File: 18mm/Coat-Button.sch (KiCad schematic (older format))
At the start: 41 parts, among them IC1 MADW__ATTINY13-MM, P1 CONN_1, P2 CONN_1, P3 CONN_1, P4 CONN_1, Q1 DMG1012T, Q2 DMG1012T

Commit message: Tweaked changes in previous commit.
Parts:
- added JP2, JP3: JUMPER, symbol JUMPER
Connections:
- wire segments 83 -> 93
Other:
- note added: "cut if transistors are used!"
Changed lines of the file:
@@
 Sheet 1 1
 Title "Coat-Button"
-Date "03 Oct 2013"
-Rev "0.22"
+Date "14 Oct 2013"
+Rev "0.23"
 Comp "2013 - blog.spitzenpfeil.org"
 Comment1 ""
@@
 Text GLabel 3350 2900 0    39   Input ~ 0
 SCK
-Wire Wire Line
-	4950 1700 5200 1700
-Wire Wire Line
-	4950 2000 5200 2000
-Connection ~ 5000 2000
-Connection ~ 5000 1700
-Wire Wire Line
-	5450 2700 5700 2700
-Wire Wire Line
-	5700 2600 5700 2750
-Wire Wire Line
-	5450 3200 5700 3200
-Wire Wire Line
-	5700 3150 5700 3300
-Connection ~ 5700 2700
-Connection ~ 5700 3200
-Wire Wire Line
-	3400 1650 3250 1650
-Wire Wire Line
-	3250 1750 3400 1750
-Wire Wire Line
-	3250 1850 3400 1850
-Wire Wire Line
-	4000 1650 4150 1650
-Wire Wire Line
-	4000 1750 4150 1750
-Wire Wire Line
-	4000 1850 4150 1850
-Wire Wire Line
-	4150 1650 4150 1550
-Wire Wire Line
-	4150 1850 4150 1950
-Wire Wire Line
-	3450 2700 3350 2700
-Wire Wire Line
-	3300 3200 3450 3200
-Wire Wire Line
-	3350 2800 3450 2800
-Wire Wire Line
-	3350 2900 3450 2900
-Wire Wire Line
-	5000 1900 5000 2100
-Wire Wire Line
-	5000 1600 5000 1800
-Wire Wire Line
-	5000 1800 4950 1800
-Wire Wire Line
-	3150 3000 3450 3000
-Wire Wire Line
-	3450 3100 3150 3100
 Text Label 3150 3000 2    60   ~ 0
 gate_a
-Wire Wire Line
-	4950 1900 5000 1900
 $Comp
 L CONN_1 P1
@@
 	0    1    1    0
 $EndComp
-Wire Wire Line
-	2300 4350 2300 4250
-Wire Wire Line
-	2300 4250 7400 4250
-Wire Wire Line
-	7400 4250 7400 4350
-Wire Wire Line
-	7200 4350 7200 4250
-Connection ~ 7200 4250
-Wire Wire Line
-	6700 4350 6700 4250
-Connection ~ 6700 4250
-Wire Wire Line
-	6500 4350 6500 4250
-Connection ~ 6500 4250
-Wire Wire Line
-	6000 4350 6000 4250
-Connection ~ 6000 4250
-Wire Wire Line
-	5800 4350 5800 4250
-Connection ~ 5800 4250
-Wire Wire Line
-	5300 4350 5300 4250
-Connection ~ 5300 4250
-Wire Wire Line
-	5100 4350 5100 4250
-Connection ~ 5100 4250
-Wire Wire Line
-	4600 4350 4600 4250
-Connection ~ 4600 4250
-Wire Wire Line
-	4400 4350 4400 4250
-Connection ~ 4400 4250
-Wire Wire Line
-	3900 4350 3900 4250
-Connection ~ 3900 4250
-Wire Wire Line
-	3700 4350 3700 4250
-Connection ~ 3700 4250
-Wire Wire Line
-	3200 4350 3200 4250
-Connection ~ 3200 4250
-Wire Wire Line
-	3000 4350 3000 4250
-Connection ~ 3000 4250
-Wire Wire Line
-	2500 4350 2500 4250
-Connection ~ 2500 4250
 $Comp
 L R R1.1
@@
 	-1   0    0    1
 $EndComp
-Wire Wire Line
-	2300 5350 2300 5500
-Wire Wire Line
-	3000 5500 3000 5350
-Wire Wire Line
-	3700 5500 3700 5350
-Connection ~ 3000 5500
-Wire Wire Line
-	4400 5500 4400 5350
-Connection ~ 3700 5500
-Wire Wire Line
-	7200 5500 7200 5350
-Connection ~ 4400 5500
-Wire Wire Line
-	6500 5350 6500 5500
-Connection ~ 6500 5500
-Wire Wire Line
-	5800 5350 5800 5500
-Connection ~ 5800 5500
-Wire Wire Line
-	5100 5350 5100 5500
-Connection ~ 5100 5500
-Wire Wire Line
-	2500 5350 2500 5600
-Wire Wire Line
-	2500 5600 8300 5600
-Wire Wire Line
-	3200 5600 3200 5350
-Wire Wire Line
-	3900 5600 3900 5350
-Connection ~ 3200 5600
-Wire Wire Line
-	4600 5600 4600 5350
-Connection ~ 3900 5600
-Wire Wire Line
-	7400 5600 7400 5350
-Connection ~ 4600 5600
-Wire Wire Line
-	6700 5350 6700 5600
-Connection ~ 6700 5600
-Wire Wire Line
-	6000 5350 6000 5600
-Connection ~ 6000 5600
-Wire Wire Line
-	5300 5350 5300 5600
-Connection ~ 5300 5600
-Connection ~ 7200 5500
-Connection ~ 7400 5600
 Text Label 3150 3100 2    60   ~ 0
 gate_b
@@
 	1    0    0    -1
 $EndComp
-Wire Wire Line
-	8300 6100 9000 6100
-Wire Wire Line
-	9000 6100 9000 5950
-Wire Wire Line
-	8650 6100 8650 6200
-Connection ~ 8650 6100
 $Comp
 L GND #PWR010
@@
 	1    0    0    -1
 $EndComp
-Wire Wire Line
-	2300 5500 9000 5500
-Wire Wire Line
-	9000 5500 9000 5550
-Wire Wire Line
-	8300 5600 8300 5650
-Wire Wire Line
-	8300 6050 8300 6100
 Text Label 7950 5950 1    60   ~ 0
 gate_a
 Text Label 8650 5850 1    60   ~ 0
 gate_b
-Wire Wire Line
-	8650 5850 8700 5850
-Wire Wire Line
-	7950 5950 8000 5950
-Text Notes 2500 5700 0    39   ~ 0
+Text Notes 2250 5750 0    39   ~ 0
 * Adjust R for about 10mA per LED\n\n(*) Rx.2 alternate footprint for single-color LED. Use instead of Rx and Rx.1
 $Comp
@@
 	1    0    0    -1
 $EndComp
-Wire Wire Line
-	2500 4850 2600 4850
-Wire Wire Line
-	2500 5350 2600 5350
-Wire Wire Line
-	3200 5350 3300 5350
-Wire Wire Line
-	3200 4850 3300 4850
-Wire Wire Line
-	3900 4850 4000 4850
-Wire Wire Line
-	3900 5350 4000 5350
 Text Notes 2650 5000 0    39   ~ 0
 (*)
 Wire Wire Line
+	4950 1700 5200 1700
+Wire Wire Line
+	4950 2000 5200 2000
+Connection ~ 5000 2000
+Connection ~ 5000 1700
+Wire Wire Line
+	5450 2700 5700 2700
+Wire Wire Line
+	5700 2600 5700 2750
+Wire Wire Line
+	5450 3200 5700 3200
+Wire Wire Line
+	5700 3150 5700 3300
+Connection ~ 5700 2700
+Connection ~ 5700 3200
+Wire Wire Line
+	3400 1650 3250 1650
+Wire Wire Line
+	3250 1750 3400 1750
+Wire Wire Line
+	3250 1850 3400 1850
+Wire Wire Line
+	4000 1650 4150 1650
+Wire Wire Line
+	4000 1750 4150 1750
+Wire Wire Line
+	4000 1850 4150 1850
+Wire Wire Line
+	4150 1650 4150 1550
+Wire Wire Line
+	4150 1850 4150 1950
+Wire Wire Line
+	3450 2700 3350 2700
+Wire Wire Line
+	3300 3200 3450 3200
+Wire Wire Line
+	3350 2800 3450 2800
+Wire Wire Line
+	3350 2900 3450 2900
+Wire Wire Line
+	5000 1900 5000 2100
+Wire Wire Line
+	5000 1600 5000 1800
+Wire Wire Line
+	5000 1800 4950 1800
+Wire Wire Line
+	3150 3000 3450 3000
+Wire Wire Line
+	3450 3100 3150 3100
+Wire Wire Line
+	4950 1900 5000 1900
+Wire Wire Line
+	2300 4350 2300 4250
+Wire Wire Line
+	2300 4250 7400 4250
+Wire Wire Line
+	7400 4250 7400 4350
+Wire Wire Line
+	7200 4350 7200 4250
+Connection ~ 7200 4250
+Wire Wire Line
+	6700 4350 6700 4250
+Connection ~ 6700 4250
+Wire Wire Line
+	6500 4350 6500 4250
+Connection ~ 6500 4250
+Wire Wire Line
+	6000 4350 6000 4250
+Connection ~ 6000 4250
+Wire Wire Line
+	5800 4350 5800 4250
+Connection ~ 5800 4250
+Wire Wire Line
+	5300 4350 5300 4250
+Connection ~ 5300 4250
+Wire Wire Line
+	5100 4350 5100 4250
+Connection ~ 5100 4250
+Wire Wire Line
+	4600 4350 4600 4250
+Connection ~ 4600 4250
+Wire Wire Line
+	4400 4350 4400 4250
+Connection ~ 4400 4250
+Wire Wire Line
+	3900 4350 3900 4250
+Connection ~ 3900 4250
+Wire Wire Line
+	3700 4350 3700 4250
+Connection ~ 3700 4250
+Wire Wire Line
+	3200 4350 3200 4250
+Connection ~ 3200 4250
+Wire Wire Line
+	3000 4350 3000 4250
+Connection ~ 3000 4250
+Wire Wire Line
+	2500 4350 2500 4250
+Connection ~ 2500 4250
+Wire Wire Line
+	2300 5350 2300 5500
+Wire Wire Line
+	3000 5500 3000 5350
+Wire Wire Line
+	3700 5500 3700 5350
+Connection ~ 3000 5500
+Wire Wire Line
+	4400 5500 4400 5350
+Connection ~ 3700 5500
+Wire Wire Line
+	7200 5500 7200 5350
+Connection ~ 4400 5500
+Wire Wire Line
+	6500 5350 6500 5500
+Connection ~ 6500 5500
+Wire Wire Line
+	5800 5350 5800 5500
+Connection ~ 5800 5500
+Wire Wire Line
+	5100 5350 5100 5800
+Connection ~ 5100 5500
+Wire Wire Line
+	2500 5350 2500 5600
+Wire Wire Line
+	2500 5600 8300 5600
+Wire Wire Line
+	3200 5600 3200 5350
+Wire Wire Line
+	3900 5600 3900 5350
+Connection ~ 3200 5600
+Wire Wire Line
+	4600 5600 4600 5350
+Connection ~ 3900 5600
+Wire Wire Line
+	7400 5600 7400 5350
+Connection ~ 4600 5600
+Wire Wire Line
+	6700 5350 6700 5600
+Connection ~ 6700 5600
+Connection ~ 6000 5600
+Wire Wire Line
+	5300 5350 5300 5600
+Connection ~ 5300 5600
+Connection ~ 7200 5500
+Connection ~ 7400 5600
+Wire Wire Line
+	8300 6100 9000 6100
+Wire Wire Line
+	9000 6100 9000 5950
+Wire Wire Line
+	8650 6100 8650 6200
+Connection ~ 8650 6100
+Wire Wire Line
+	2300 5500 9000 5500
+Wire Wire Line
+	9000 5500 9000 5550
+Wire Wire Line
+	8300 5600 8300 5650
+Wire Wire Line
+	8300 6050 8300 6100
+Wire Wire Line
+	8650 5850 8700 5850
+Wire Wire Line
+	7950 5950 8000 5950
+Wire Wire Line
+	2500 4850 2600 4850
+Wire Wire Line
+	2500 5350 2600 5350
+Wire Wire Line
+	3200 5350 3300 5350
+Wire Wire Line
+	3200 4850 3300 4850
+Wire Wire Line
+	3900 4850 4000 4850
+Wire Wire Line
+	3900 5350 4000 5350
+Wire Wire Line
 	4600 4850 4700 4850
 Wire Wire Line
@@
 Wire Wire Line
 	7400 5350 7500 5350
+$Comp
+L JUMPER JP3
+U 1 1 525C0CD5
+P 6000 6100
+F 0 "JP3" H 6000 6250 60  0000 C CNN
+F 1 "JUMPER" H 6000 6020 40  0000 C CNN
+F 2 "" H 6000 6100 60  0000 C CNN
+F 3 "" H 6000 6100 60  0000 C CNN
+	1    6000 6100
+	0    1    1    0
+$EndComp
+Wire Wire Line
+	6000 6400 6000 6500
+Wire Wire Line
+	5100 6400 5100 6500
+Text Label 6100 6500 0    60   ~ 0
+gate_a
+Text Label 5200 6500 0    60   ~ 0
+gate_b
+Wire Wire Line
+	6000 6500 6100 6500
+Wire Wire Line
+	5100 6500 5200 6500
+Wire Wire Line
+	5800 5800 5800 6400
+Wire Wire Line
+	5800 6400 6000 6400
+Wire Wire Line
+	6000 5350 6000 5800
+Wire Wire Line
+	6000 5800 5800 5800
+Wire Wire Line
+	5100 5800 4900 5800
+Wire Wire Line
+	4900 5800 4900 6400
+Wire Wire Line
+	4900 6400 5100 6400
+Text Notes 4050 6400 0    39   ~ 0
+cut if transistors are used!
+$Comp
+L JUMPER JP2
+U 1 1 525C1412
+P 5100 6100
+F 0 "JP2" H 5100 6250 60  0000 C CNN
+F 1 "JUMPER" H 5100 6020 40  0000 C CNN
+F 2 "" H 5100 6100 60  0000 C CNN
+F 3 "" H 5100 6100 60  0000 C CNN
+	1    5100 6100
+	0    1    1    0
+$EndComp
 $EndSCHEMATC

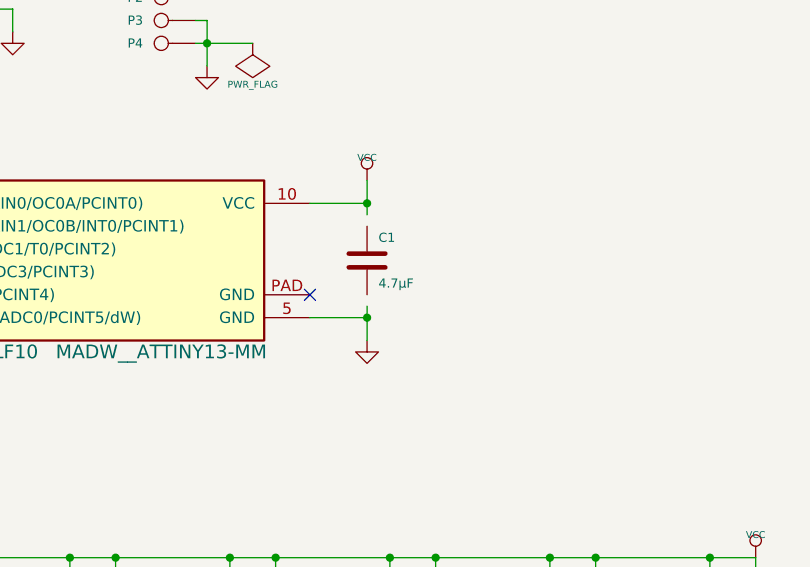
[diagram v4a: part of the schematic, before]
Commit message: Moved capacitor + tweaks.
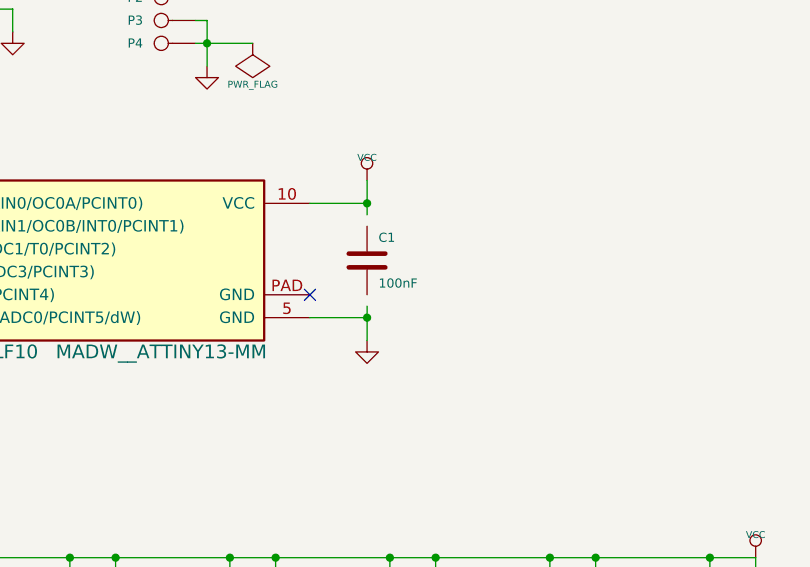
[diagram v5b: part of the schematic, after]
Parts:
- C1: value 4.7µF -> 100nF
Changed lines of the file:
@@
 P 5700 2950
 F 0 "C1" H 5750 3050 40  0000 L CNN
-F 1 "4.7µF" H 5750 2850 40  0000 L CNN
+F 1 "100nF" H 5750 2850 40  0000 L CNN
 F 2 "" H 5738 2800 30  0000 C CNN
 F 3 "" H 5700 2950 60  0000 C CNN

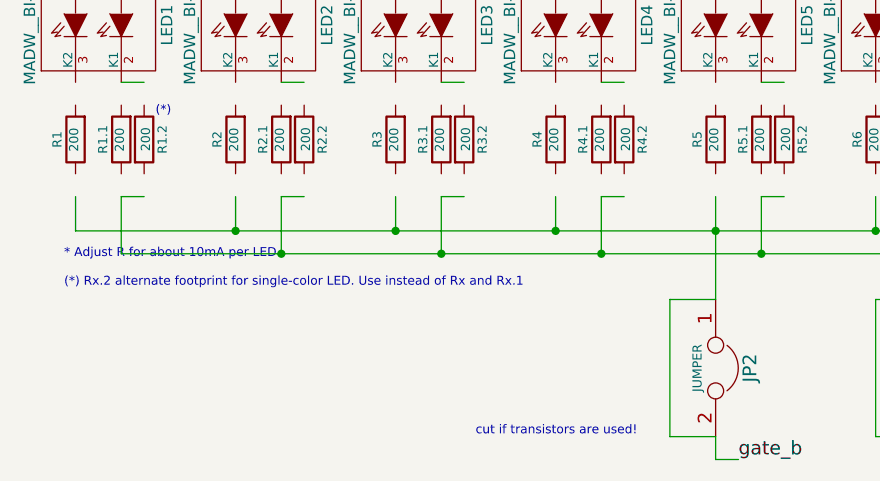
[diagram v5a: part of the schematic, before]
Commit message: Added a comment to the schematic (LED resistors).
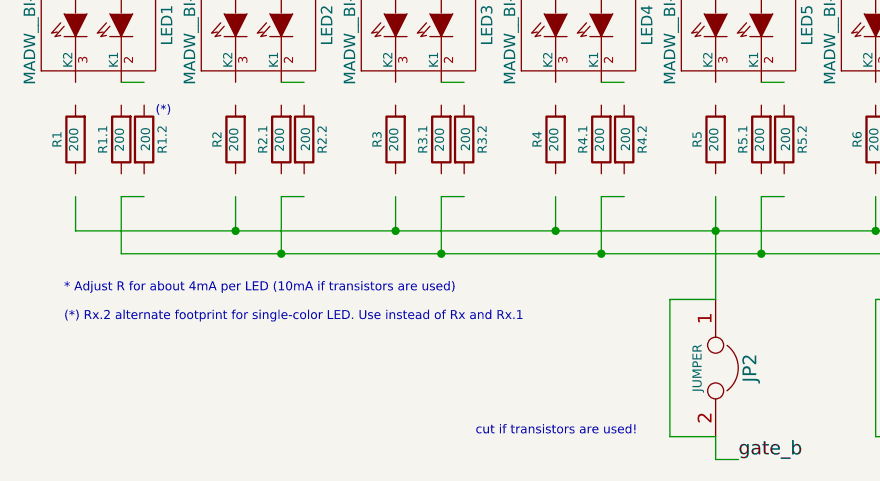
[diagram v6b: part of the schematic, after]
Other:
- note added: "* Adjust R for about 4mA per LED (10mA if transistors are used)\n\n(*) Rx.2 alternate footprint for single-color LED. Use instead of Rx and Rx.1"
- note removed: "* Adjust R for about 10mA per LED\n\n(*) Rx.2 alternate footprint for single-color LED. Use instead of Rx and Rx.1"
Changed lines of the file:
@@
 Text Label 8650 5850 1    60   ~ 0
 gate_b
-Text Notes 2250 5750 0    39   ~ 0
-* Adjust R for about 10mA per LED\n\n(*) Rx.2 alternate footprint for single-color LED. Use instead of Rx and Rx.1
+Text Notes 2250 5900 0    39   ~ 0
+* Adjust R for about 4mA per LED (10mA if transistors are used)\n\n(*) Rx.2 alternate footprint for single-color LED. Use instead of Rx and Rx.1
 $Comp
 L R R1.2

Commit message: Getting started with charlieplexing.
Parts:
- removed JP2, JP3: JUMPER, symbol JUMPER
- removed LED1, LED2, LED3, LED4, LED5, LED6, LED7, LED8: MADW__BI-LED, symbol MADW__BI-LED
- removed Q1, Q2: DMG1012T, SOT523, symbol MOSFET_N
- removed R1.1, R1.2, R2.1, R2.2, R3.1, R3.2, R4.1, R4.2, R5.1, R5.2, R6.1, R6.2, R7.1, R7.2, R8.1, R8.2: 200, symbol R
- added D1, D2, D3, D4, D5, D6, D7, D8: LED, my_parts:MADW__CHIPLED-0805, symbol LED
- C1: value 100nF -> 4.7µF; footprint (none) -> my_parts:MADW__C0805
- IC1: footprint MADW__MLF10 -> my_parts:MADW__MLF10
- JP1: footprint (none) -> DIL-Headers:DIL-3_1.27mm
- P1, P2, P3, P4: footprint (none) -> SIL-Headers:SIL-1
- R1, R2, R3, R4, R5, R6, R7, R8: value 200 -> R; footprint (none) -> my_parts:MADW__R0603
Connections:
- net labels added: CPLEX_0, CPLEX_1, CPLEX_2, CPLEX_3, RESET
- net labels removed: MISO, MOSI, RST, SCK, gate_a, gate_b
- wire segments 93 -> 48
- no-connect marks 1 -> 2
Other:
- note removed: "(*)"
- note removed: "* Adjust R for about 4mA per LED (10mA if transistors are used)\n\n(*) Rx.2 alternate footprint for single-color LED. Use instead of Rx and Rx.1"
- note removed: "cut if transistors are used!"
